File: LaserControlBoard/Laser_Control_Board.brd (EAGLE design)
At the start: 50.8 x 50.8 mm, 22 parts, among them J1 Servo Header, J2 FTDI Header, U1 ATMEGA328P_TQFP, Y1 16MHz

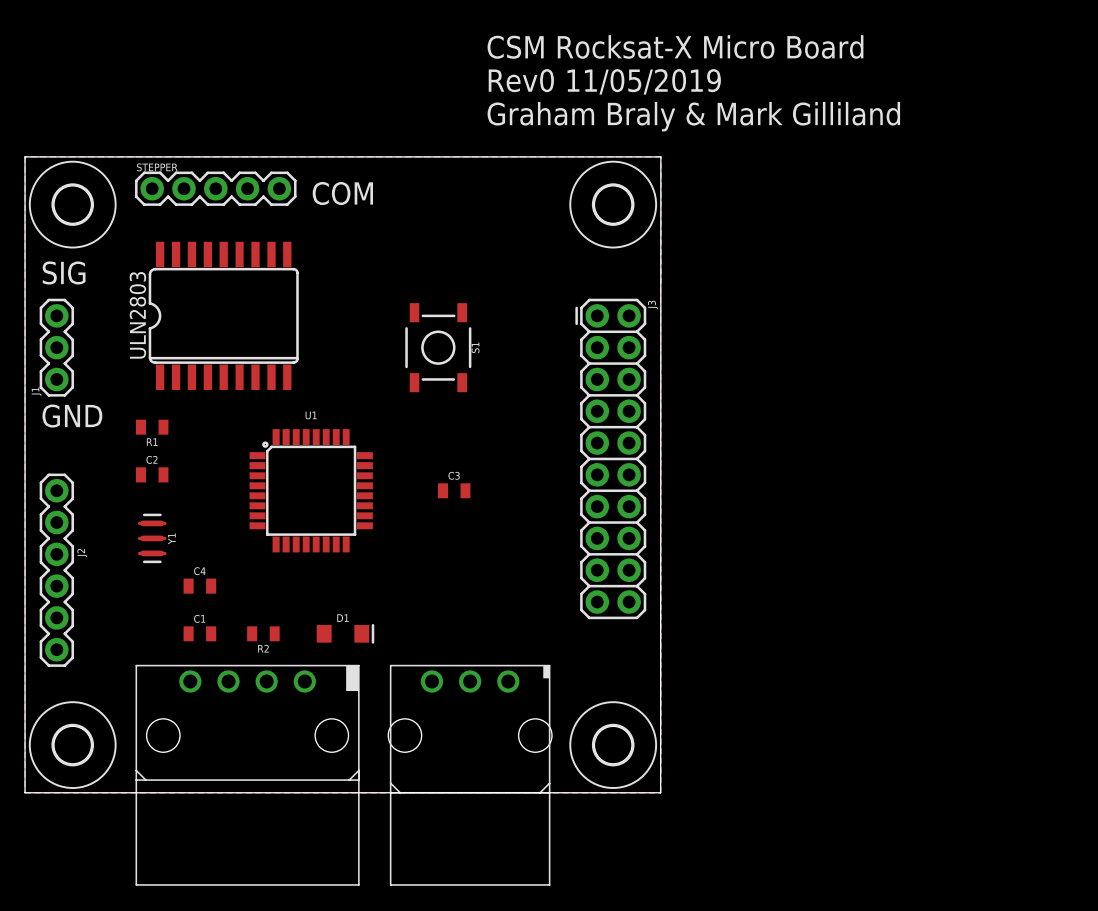
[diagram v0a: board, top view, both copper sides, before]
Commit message: Added Mosfet to library. First rev of subsystem control board finished and routed.
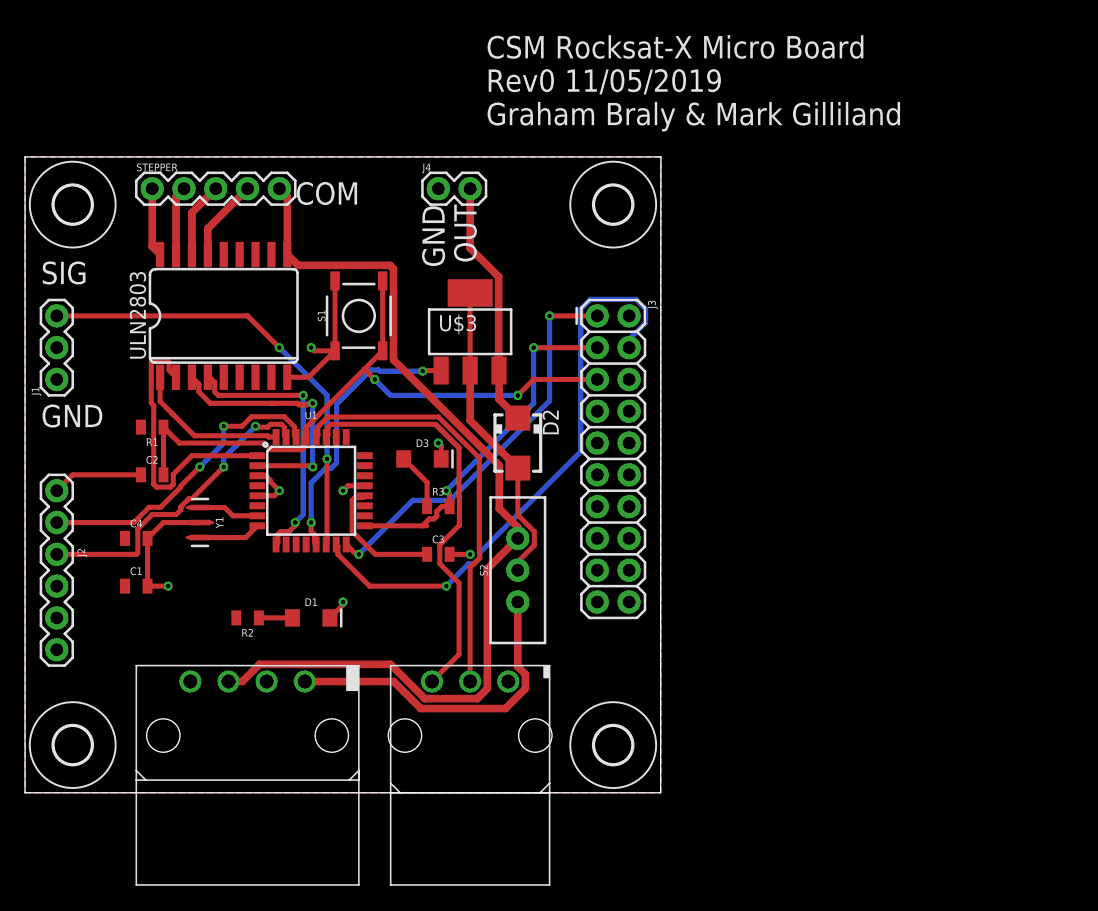
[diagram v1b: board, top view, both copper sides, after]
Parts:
- added D2: S1M, diode:SMA
- added D3: GREEN, SparkFun-LED:LED-1206
- added J4: (no value), SparkFun-Connectors:1X02
- added R3: 1kΩ, SparkFun-Resistors:0805
- added S2: (no value), SparkFun-Switches:SWITCH_SPDT_PTH_11.6X4.0MM
- added U$3: BUK9880-55A, PowerManagementParts:SOT223
- D1: value (none) -> GREEN
- R2: value (none) -> 1kΩ
- moved S1 6.84 mm to (26.7, 38.1), turned to 90 degrees
- moved C1 6.35 mm to (8.89, 16.5)
- moved C4 6.35 mm to (8.89, 20.3)
- moved C3 5.24 mm to (33.0, 19.1)
- moved Y1 4.02 mm to (14.0, 21.6)
- moved D1 2.84 mm to (22.9, 14.0)
- moved R2 1.80 mm to (17.8, 14.0)
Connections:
- new net MOSFET_OUT: D2.C, J4.2, U$3.3
- new net N$1: D2.A, S2.2, U$3.2, U$3.4
- new net N$7: D3.A, R3.1
- new net PB1: U$3.1, U1.13
- net 12V: now also S2.3
- net 5V_ACT: now also S2.1
- net GND: now also D3.C, J4.1
- net SCK: now also R3.2
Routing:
- net 5V_ACT: track 0.00 -> 76.6 mm
- net RESET: track 0.00 -> 51.8 mm, vias 0 -> 2
- net MOSI: track 0.00 -> 46.9 mm, vias 0 -> 1
- net PB2: track 0.00 -> 36.2 mm, vias 0 -> 2
- net SDA: track 0.00 -> 35.7 mm
- net SCL: track 0.00 -> 33.7 mm
- net GND: track 0.00 -> 33.3 mm, vias 0 -> 7
- net MISO: track 0.00 -> 32.3 mm, vias 0 -> 2
- net SCK: track 0.00 -> 28.7 mm, vias 0 -> 2
- net 12V: track 0.00 -> 26.4 mm
- net TXO: track 0.00 -> 25.2 mm, vias 0 -> 2
- net N$1: track 0.00 -> 24.8 mm
- net RXI: track 0.00 -> 24.5 mm, vias 0 -> 2
- net PD3: track 0.00 -> 22.7 mm
- net PB1: track 0.00 -> 22.0 mm, vias 0 -> 2
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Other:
- board text added: "OUT"

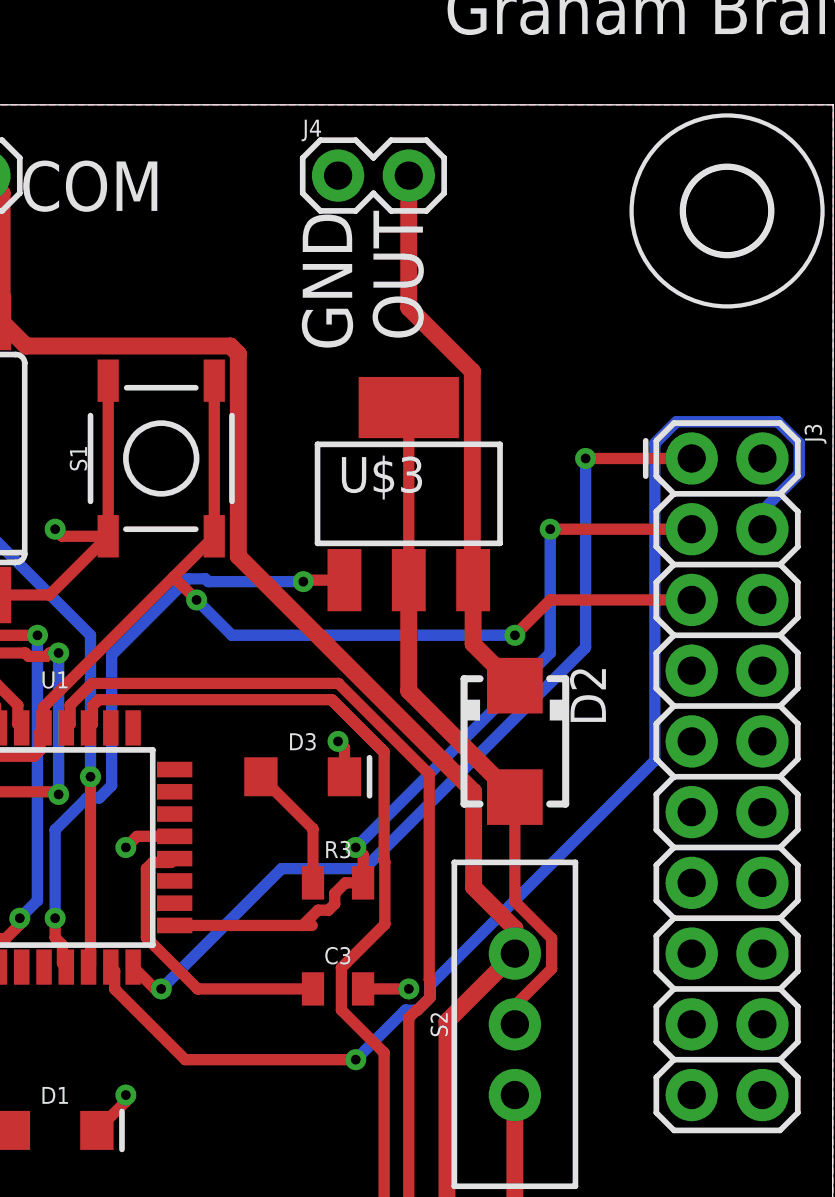
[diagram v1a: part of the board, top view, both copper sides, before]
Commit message: Redid MOSFET symbol. MOSFET is now Nchan on Low-side.
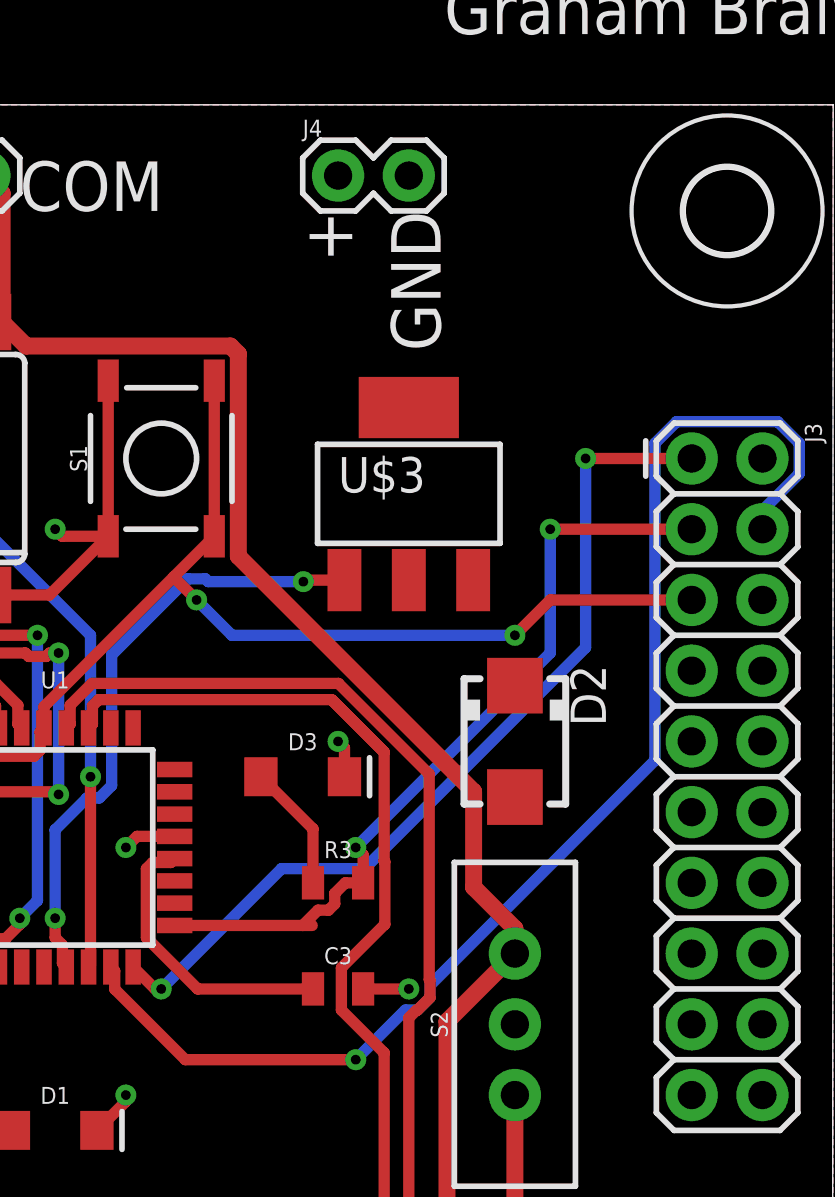
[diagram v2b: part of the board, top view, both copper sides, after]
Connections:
- removed net MOSFET_OUT: D2.C, J4.2, U$3.3
- new net MOSFET_SWITCHED: D2.C, J4.2, U$3.2, U$3.4
- net GND: now also D2.A, U$3.3; no longer J4.1
- net N$1: now also J4.1; no longer D2.A, U$3.2, U$3.4
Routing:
- net N$1: track 24.8 -> 0.00 mm
- net MOSFET_OUT: track 20.0 -> 0.00 mm
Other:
- board text added: "+"
- board text removed: "OUT"
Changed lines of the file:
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@@
 Graham Braly &amp; Mark Gilliland</text>
 <text x="21.59" y="46.99" size="1.778" layer="25">COM</text>
-<text x="31.75" y="46.99" size="1.778" layer="25" rot="R270">GND</text>
-<text x="34.29" y="46.99" size="1.778" layer="25" rot="R270">OUT</text>
+<text x="34.925" y="46.99" size="1.778" layer="25" rot="R270">GND</text>
+<text x="31.75" y="46.99" size="1.778" layer="25" rot="R270">+</text>
 </plain>
 <attributes>
@@
 <element name="U$2" library="PowerManagementParts" package="MOLEX_3PIN" value="MOLEX_3PIN" x="35.56" y="8.89"/>
 <element name="FRAME1" library="SparkFun-Aesthetics" package="DUMMY" value="FRAME-LETTERNO_PACKAGE" x="0" y="0">
-<attribute name="DESIGNER" value="Nobody" x="0" y="0" size="1.778" layer="27" display="off"/>
-<attribute name="VERSION" value="v01" x="0" y="0" size="1.778" layer="27" display="off"/>
+<attribute name="DESIGNER" value="Mines RockSat-X" x="0" y="0" size="1.778" layer="27" display="off"/>
+<attribute name="VERSION" value="1" x="0" y="0" size="1.778" layer="27" display="off"/>
 </element>
 <element name="R2" library="SparkFun-Resistors" package="0805" value="1kΩ" x="17.78" y="13.97" rot="R180">
@@
 <attribute name="SF_SKU" value="COM-08720" x="26.67" y="38.1" size="1.778" layer="27" rot="R90" display="off"/>
 </element>
-<element name="D2" library="diode" library_urn="urn:adsk.eagle:library:210" package="SMA" package3d_urn="urn:adsk.eagle:package:43460/3" value="S1M" x="39.37" y="27.94" rot="R270">
-<attribute name="POPULARITY" value="0" x="39.37" y="27.94" size="1.778" layer="27" rot="R270" display="off"/>
-</element>
+<element name="D2" library="diode" library_urn="urn:adsk.eagle:library:210" package="SMA" package3d_urn="urn:adsk.eagle:package:43460/3" value="S1M" x="39.37" y="27.94" rot="R270"/>
 <element name="D1" library="SparkFun-LED" package="LED-1206" value="GREEN" x="22.86" y="13.97">
 <attribute name="PROD_ID" value="DIO-00862" x="22.86" y="13.97" size="1.778" layer="27" display="off"/>
@@
 <contactref element="S1" pad="1"/>
 <contactref element="D1" pad="C"/>
-<contactref element="J4" pad="1"/>
 <contactref element="D3" pad="C"/>
 <wire x1="13.97" y1="21.59" x2="11.06" y2="21.59" width="0.4064" layer="1"/>
@@
 <wire x1="19.2206125" y1="25.33" x2="19.5834" y2="24.9672125" width="0.4064" layer="1"/>
 <wire x1="24.765" y1="40.894" x2="24.765" y2="35.306" width="0.4064" layer="1"/>
+<contactref element="D2" pad="A"/>
+<contactref element="U$3" pad="3"/>
+<wire x1="37.871" y1="33.731" x2="48.26" y2="33.02" width="0" layer="19" extent="1-1"/>
+<wire x1="33.02" y1="27.94" x2="37.871" y2="33.731" width="0" layer="19" extent="1-1"/>
+<wire x1="39.37" y1="25.94" x2="33.25" y2="26.67" width="0" layer="19" extent="1-1"/>
+<wire x1="27.1526" y1="24.53" x2="33.25" y2="26.67" width="0" layer="19" extent="1-1"/>
+<wire x1="20.32" y1="24.13" x2="25.4" y2="24.13" width="0" layer="19" extent="1-1"/>
+<wire x1="13.97" y1="21.59" x2="18.5674" y2="23.73" width="0" layer="19" extent="1-1"/>
+<wire x1="33.92" y1="19.05" x2="33.25" y2="26.67" width="0" layer="19" extent="1-1"/>
+<wire x1="20.955" y1="33.1978" x2="19.2206125" y2="25.33" width="0" layer="19" extent="1-1"/>
+<wire x1="2.54" y1="11.43" x2="9.79" y2="16.51" width="0" layer="19" extent="1-1"/>
+<wire x1="25.4" y1="15.24" x2="25.4" y2="24.13" width="0" layer="19" extent="1-1"/>
+<wire x1="19.304" y1="8.89" x2="24.36" y2="13.97" width="0" layer="19" extent="1-1"/>
+<wire x1="38.608" y1="8.89" x2="35.56" y2="19.05" width="0" layer="19" extent="1-1"/>
+<wire x1="2.54" y1="33.02" x2="11.06" y2="21.59" width="0" layer="19" extent="1-1"/>
 </signal>
 <signal name="DTR">
@@
 <wire x1="15.1638" y1="32.0239875" x2="15.4377875" y2="31.75" width="0.4064" layer="1"/>
 </signal>
-<signal name="N$1">
-<contactref element="S2" pad="2"/>
-<contactref element="U$3" pad="2"/>
-<contactref element="U$3" pad="4"/>
-<contactref element="D2" pad="A"/>
-<wire x1="35.56" y1="33.731" x2="35.56" y2="29.75" width="0.6096" layer="1"/>
-<wire x1="35.56" y1="29.75" x2="39.37" y2="25.94" width="0.6096" layer="1"/>
-<wire x1="35.56" y1="39.929" x2="35.56" y2="33.731" width="0.4064" layer="1"/>
-<wire x1="39.37" y1="25.94" x2="39.37" y2="22.18789375" width="0.4064" layer="1"/>
-<wire x1="40.6908" y1="20.86709375" x2="40.6908" y2="19.77290625" width="0.4064" layer="1"/>
-<wire x1="39.37" y1="22.18789375" x2="40.6908" y2="20.86709375" width="0.4064" layer="1"/>
-<wire x1="39.37" y1="18.45210625" x2="39.37" y2="17.78" width="0.4064" layer="1"/>
-<wire x1="40.6908" y1="19.77290625" x2="39.37" y2="18.45210625" width="0.4064" layer="1"/>
-</signal>
-<signal name="MOSFET_OUT">
-<contactref element="D2" pad="C"/>
-<contactref element="U$3" pad="3"/>
-<contactref element="J4" pad="2"/>
-<wire x1="37.8172" y1="33.7848" x2="37.871" y2="33.731" width="0.6096" layer="1"/>
-<wire x1="37.871" y1="33.731" x2="37.871" y2="31.439" width="0.6096" layer="1"/>
-<wire x1="37.871" y1="31.439" x2="39.37" y2="29.94" width="0.6096" layer="1"/>
-<wire x1="35.56" y1="48.26" x2="35.56" y2="43.5115" width="0.6096" layer="1"/>
-<wire x1="35.56" y1="43.5115" x2="37.8426" y2="41.2289" width="0.6096" layer="1"/>
-<wire x1="37.8426" y1="33.7594" x2="37.871" y2="33.731" width="0.6096" layer="1"/>
-<wire x1="37.8426" y1="41.2289" x2="37.8426" y2="33.7594" width="0.6096" layer="1"/>
-</signal>
 <signal name="PB1">
 <contactref element="U1" pad="13"/>
@@
 <wire x1="32.12" y1="24.8" x2="32.12" y2="22.86" width="0.4064" layer="1"/>
 </signal>
+<signal name="N$1">
+<contactref element="S2" pad="2"/>
+<contactref element="J4" pad="1"/>
+<wire x1="39.37" y1="17.78" x2="33.02" y2="48.26" width="0" layer="19" extent="1-1"/>
+</signal>
+<signal name="MOSFET_SWITCHED">
+<contactref element="J4" pad="2"/>
+<contactref element="U$3" pad="2"/>
+<contactref element="U$3" pad="4"/>
+<contactref element="D2" pad="C"/>
+<wire x1="35.56" y1="39.929" x2="35.56" y2="48.26" width="0" layer="19" extent="1-1"/>
+<wire x1="35.56" y1="33.731" x2="35.56" y2="39.929" width="0" layer="19" extent="1-1"/>
+<wire x1="39.37" y1="29.94" x2="35.56" y2="33.731" width="0" layer="19" extent="1-1"/>
+</signal>
 </signals>
